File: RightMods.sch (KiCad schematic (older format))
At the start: 15 parts

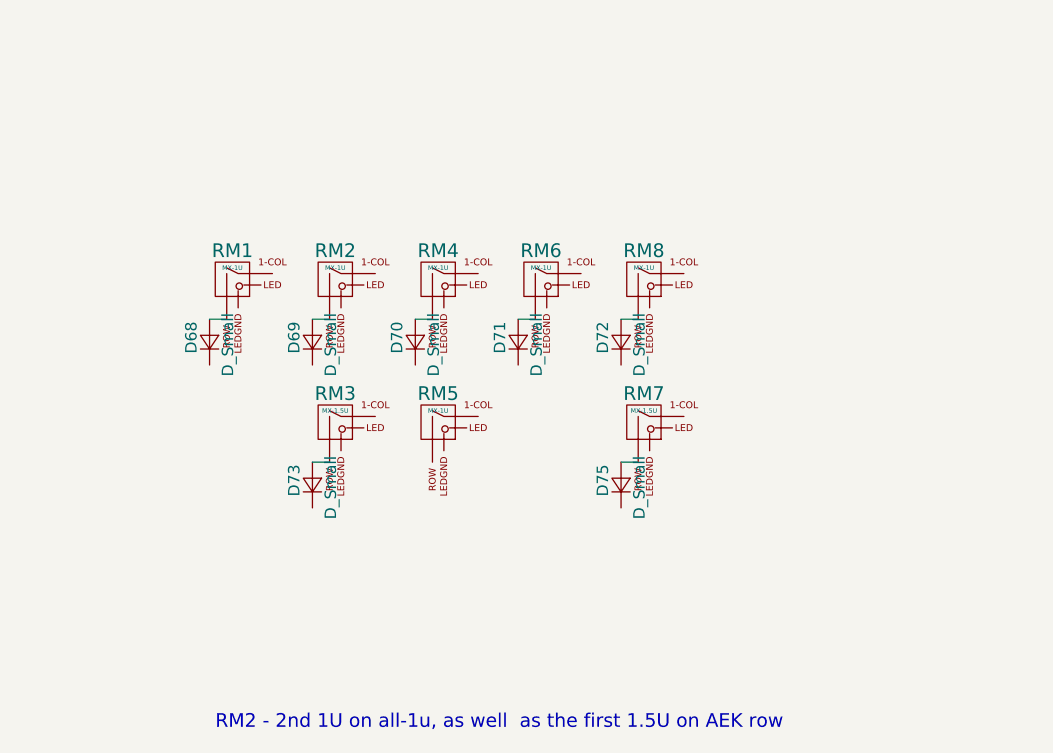
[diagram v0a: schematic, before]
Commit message: Place diodes, remove duplicates
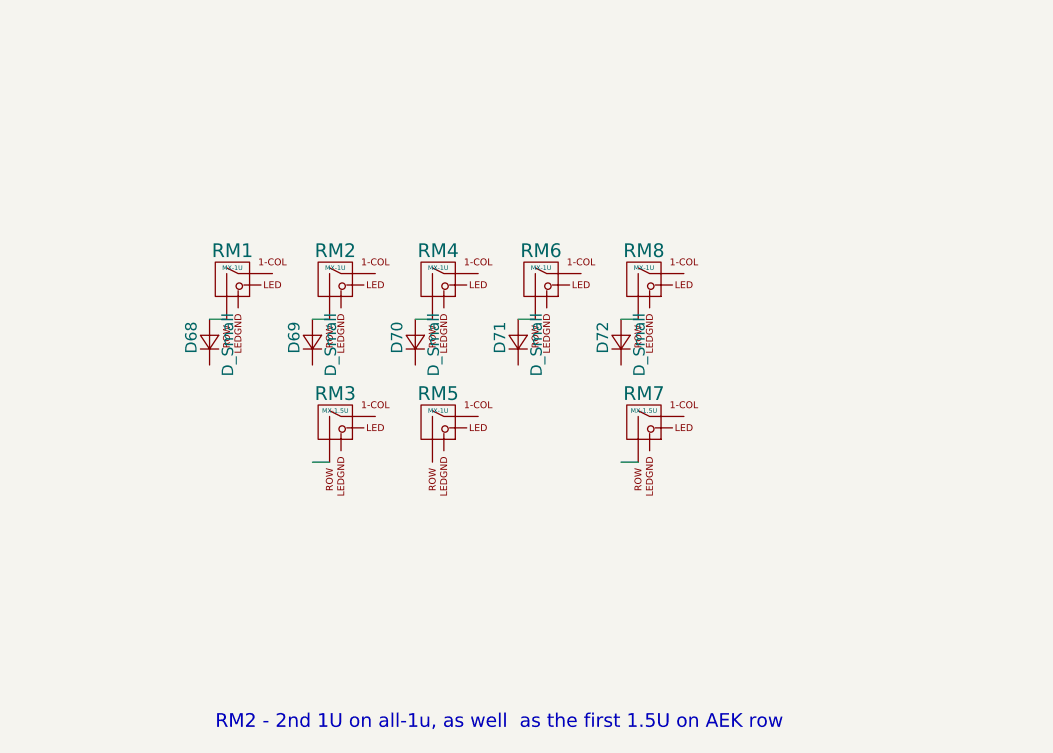
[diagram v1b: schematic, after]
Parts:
- removed D73, D75: D_Small, Diodes_SMD:D_SOD-123, symbol D_Small
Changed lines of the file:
@@
 	1    0    0    -1
-$EndComp
-$Comp
-L D_Small D73
-U 1 1 5A696AC3
-P 2525 3350
-F 0 "D73" H 2475 3430 50  0000 L CNN
-F 1 "D_Small" H 2375 3270 50  0000 L CNN
-F 2 "Diodes_SMD:D_SOD-123" V 2525 3350 50  0001 C CNN
-F 3 "" V 2525 3350 50  0001 C CNN
-	1    2525 3350
-	0    -1   -1   0
 $EndComp
 Wire Wire Line
@@
 	1    0    0    -1
 $EndComp
-$Comp
-L D_Small D75
-U 1 1 5A696AF0
-P 3875 3350
-F 0 "D75" H 3825 3430 50  0000 L CNN
-F 1 "D_Small" H 3725 3270 50  0000 L CNN
-F 2 "Diodes_SMD:D_SOD-123" V 3875 3350 50  0001 C CNN
-F 3 "" V 3875 3350 50  0001 C CNN
-	1    3875 3350
-	0    -1   -1   0
-$EndComp
 Wire Wire Line

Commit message: Add basic row col to subsheets
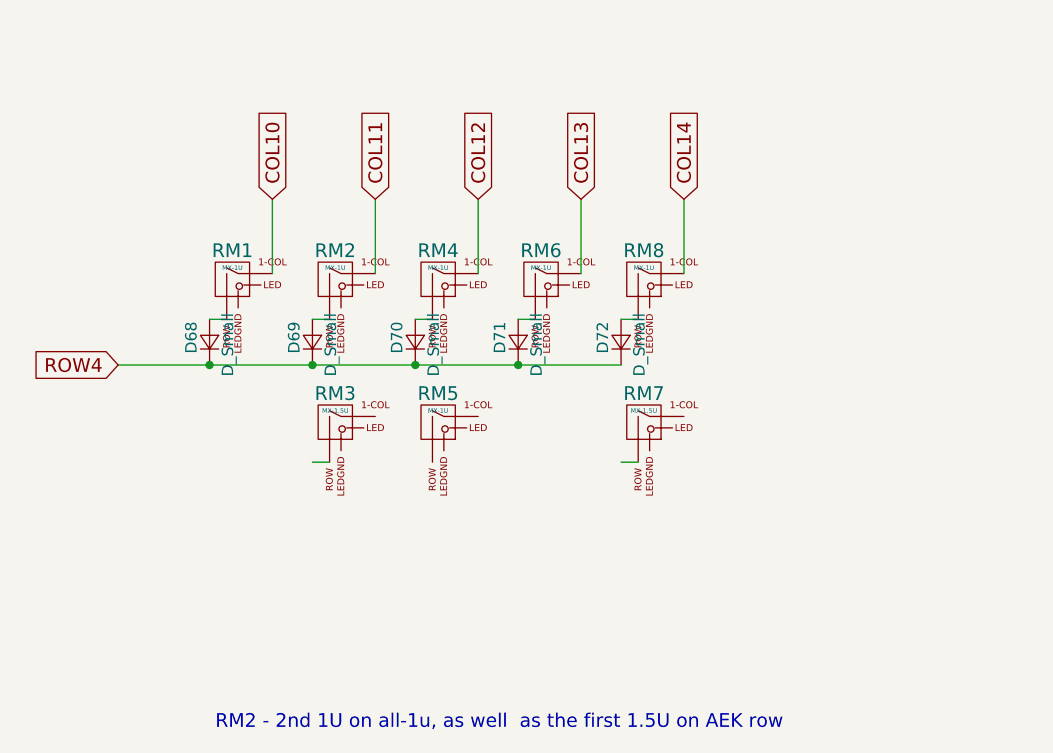
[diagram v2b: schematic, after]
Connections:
- net labels added: COL10, COL11, COL12, COL13, COL14, ROW4
- wire segments 7 -> 13
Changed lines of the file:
@@
 	1    0    0    -1
 $EndComp
+Wire Wire Line
+	4150 2425 4150 2100
+Text GLabel 4150 2100 1    60   Input ~ 0
+COL14
+Wire Wire Line
+	3700 2425 3700 2100
+Text GLabel 3700 2100 1    60   Input ~ 0
+COL13
+Wire Wire Line
+	3250 2425 3250 2100
+Text GLabel 3250 2100 1    60   Input ~ 0
+COL12
+Wire Wire Line
+	2800 2425 2800 2100
+Text GLabel 2800 2100 1    60   Input ~ 0
+COL11
+Wire Wire Line
+	2350 2425 2350 2100
+Text GLabel 2350 2100 1    60   Input ~ 0
+COL10
+Wire Wire Line
+	1675 2825 3875 2825
+Connection ~ 2525 2825
+Connection ~ 2975 2825
+Connection ~ 3425 2825
+Connection ~ 2075 2825
+Text GLabel 1675 2825 0    60   Input ~ 0
+ROW4
 $EndSCHEMATC

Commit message: Pinout right mods
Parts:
- RM3, RM7: footprint MX_Alps_Hybrid:MX-1.5U -> MX_Alps_Hybrid:MX-1.5U-FLIPPED
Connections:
- wire segments 13 -> 25
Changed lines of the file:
@@
 $EndComp
 Wire Wire Line
-	2600 2625 2525 2625
+	2400 2625 2600 2625
 $Comp
 L MX-1U RM4
@@
 $EndComp
 Wire Wire Line
-	3050 2625 2975 2625
+	2900 2625 3050 2625
 $Comp
 L MX-1U RM6
@@
 $EndComp
 Wire Wire Line
-	3950 2625 3875 2625
+	3750 2625 3950 2625
 $Comp
 L MX-1U RM3
@@
 F 0 "RM3" H 2625 3200 60  0000 C CNN
 F 1 "MX-1.5U" H 2625 3125 20  0000 C CNN
-F 2 "MX_Alps_Hybrid:MX-1.5U" H 2600 3050 60  0001 C CNN
+F 2 "MX_Alps_Hybrid:MX-1.5U-FLIPPED" H 2600 3050 60  0001 C CNN
 F 3 "" H 2600 3050 60  0001 C CNN
 	1    2625 3075
 	1    0    0    -1
 $EndComp
-Wire Wire Line
-	2600 3250 2525 3250
 $Comp
 L MX-1U RM7
@@
 F 0 "RM7" H 3975 3200 60  0000 C CNN
 F 1 "MX-1.5U" H 3975 3125 20  0000 C CNN
-F 2 "MX_Alps_Hybrid:MX-1.5U" H 3950 3050 60  0001 C CNN
+F 2 "MX_Alps_Hybrid:MX-1.5U-FLIPPED" H 3950 3050 60  0001 C CNN
 F 3 "" H 3950 3050 60  0001 C CNN
 	1    3975 3075
 	1    0    0    -1
 $EndComp
-Wire Wire Line
-	3950 3250 3875 3250
 Text Notes 2100 4425 0    60   ~ 0
 RM2 - 2nd 1U on all-1u, as well  as the first 1.5U on AEK row
@@
 COL13
 Wire Wire Line
-	3250 2425 3250 2100
+	3250 2100 3250 3050
 Text GLabel 3250 2100 1    60   Input ~ 0
 COL12
@@
 Text GLabel 1675 2825 0    60   Input ~ 0
 ROW4
+Wire Wire Line
+	2800 3050 2800 2900
+Wire Wire Line
+	2800 2900 2400 2900
+Wire Wire Line
+	2400 2900 2400 2625
+Connection ~ 2525 2625
+Wire Wire Line
+	2600 3250 2850 3250
+Wire Wire Line
+	2850 3250 2850 2425
+Wire Wire Line
+	2850 2425 2800 2425
+Connection ~ 3250 2425
+Wire Wire Line
+	3050 3250 2900 3250
+Wire Wire Line
+	2900 3250 2900 2625
+Connection ~ 2975 2625
+Wire Wire Line
+	4150 3050 4150 2900
+Wire Wire Line
+	4150 2900 3750 2900
+Wire Wire Line
+	3750 2900 3750 2625
+Connection ~ 3875 2625
+Wire Wire Line
+	3950 3250 4200 3250
+Wire Wire Line
+	4200 3250 4200 2425
+Wire Wire Line
+	4200 2425 4150 2425
 $EndSCHEMATC

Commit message: Swap footprints for No-LED counterparts
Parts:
- RM1, RM2, RM4, RM5, RM6, RM8: footprint MX_Alps_Hybrid:MX-1U -> MX_Alps_Hybrid:MX-1U-NoLED
- RM3, RM7: footprint MX_Alps_Hybrid:MX-1.5U-FLIPPED -> MX_Alps_Hybrid:MX-1.5U-NoLED
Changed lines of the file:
@@
 F 0 "RM1" H 2175 2575 60  0000 C CNN
 F 1 "MX-1U" H 2175 2500 20  0000 C CNN
-F 2 "MX_Alps_Hybrid:MX-1U" H 2150 2425 60  0001 C CNN
+F 2 "MX_Alps_Hybrid:MX-1U-NoLED" H 2150 2425 60  0001 C CNN
 F 3 "" H 2150 2425 60  0001 C CNN
 	1    2175 2450
@@
 F 0 "RM2" H 2625 2575 60  0000 C CNN
 F 1 "MX-1U" H 2625 2500 20  0000 C CNN
-F 2 "MX_Alps_Hybrid:MX-1U" H 2600 2425 60  0001 C CNN
+F 2 "MX_Alps_Hybrid:MX-1U-NoLED" H 2600 2425 60  0001 C CNN
 F 3 "" H 2600 2425 60  0001 C CNN
 	1    2625 2450
@@
 F 0 "RM4" H 3075 2575 60  0000 C CNN
 F 1 "MX-1U" H 3075 2500 20  0000 C CNN
-F 2 "MX_Alps_Hybrid:MX-1U" H 3050 2425 60  0001 C CNN
+F 2 "MX_Alps_Hybrid:MX-1U-NoLED" H 3050 2425 60  0001 C CNN
 F 3 "" H 3050 2425 60  0001 C CNN
 	1    3075 2450
@@
 F 0 "RM6" H 3525 2575 60  0000 C CNN
 F 1 "MX-1U" H 3525 2500 20  0000 C CNN
-F 2 "MX_Alps_Hybrid:MX-1U" H 3500 2425 60  0001 C CNN
+F 2 "MX_Alps_Hybrid:MX-1U-NoLED" H 3500 2425 60  0001 C CNN
 F 3 "" H 3500 2425 60  0001 C CNN
 	1    3525 2450
@@
 F 0 "RM8" H 3975 2575 60  0000 C CNN
 F 1 "MX-1U" H 3975 2500 20  0000 C CNN
-F 2 "MX_Alps_Hybrid:MX-1U" H 3950 2425 60  0001 C CNN
+F 2 "MX_Alps_Hybrid:MX-1U-NoLED" H 3950 2425 60  0001 C CNN
 F 3 "" H 3950 2425 60  0001 C CNN
 	1    3975 2450
@@
 F 0 "RM3" H 2625 3200 60  0000 C CNN
 F 1 "MX-1.5U" H 2625 3125 20  0000 C CNN
-F 2 "MX_Alps_Hybrid:MX-1.5U-FLIPPED" H 2600 3050 60  0001 C CNN
+F 2 "MX_Alps_Hybrid:MX-1.5U-NoLED" H 2600 3050 60  0001 C CNN
 F 3 "" H 2600 3050 60  0001 C CNN
 	1    2625 3075
@@
 F 0 "RM7" H 3975 3200 60  0000 C CNN
 F 1 "MX-1.5U" H 3975 3125 20  0000 C CNN
-F 2 "MX_Alps_Hybrid:MX-1.5U-FLIPPED" H 3950 3050 60  0001 C CNN
+F 2 "MX_Alps_Hybrid:MX-1.5U-NoLED" H 3950 3050 60  0001 C CNN
 F 3 "" H 3950 3050 60  0001 C CNN
 	1    3975 3075
@@
 F 0 "RM5" H 3075 3200 60  0000 C CNN
 F 1 "MX-1U" H 3075 3125 20  0000 C CNN
-F 2 "MX_Alps_Hybrid:MX-1U" H 3050 3050 60  0001 C CNN
+F 2 "MX_Alps_Hybrid:MX-1U-NoLED" H 3050 3050 60  0001 C CNN
 F 3 "" H 3050 3050 60  0001 C CNN
 	1    3075 3075

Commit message: Update right mods
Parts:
- removed D68, D69, D70, D71, D72: D_Small, Diodes_SMD:D_SOD-123, symbol D_Small
- added RM9: MX-1U, symbol MX-1U
- RM1, RM2, RM4, RM5, RM6, RM8: footprint MX_Alps_Hybrid:MX-1U-NoLED -> (none)
- RM3, RM7: value MX-1.5U -> MX-1U; footprint MX_Alps_Hybrid:MX-1.5U-NoLED -> (none)
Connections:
- net COL11: no longer RM3.2 (ROW)
- net COL12: no longer RM5.1 (COL)
- net COL13: now also RM7.1 (COL); no longer RM6.1 (COL)
- net COL14: now also RM9.1 (COL); no longer RM7.2 (ROW), RM8.1 (COL)
- net ROW4: now also RM2.2 (ROW), RM4.2 (ROW), RM7.2 (ROW), RM9.2 (ROW)
- net at RM3.1 (COL): no longer RM2.2 (ROW)
- net at RM5.2 (ROW): no longer RM4.2 (ROW)
- net at RM8.2 (ROW): no longer RM7.1 (COL)
- net COL10: no longer names the net of RM1.1 (COL)
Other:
- note removed: "RM2 - 2nd 1U on all-1u, as well as the first 1.5U on AEK row"

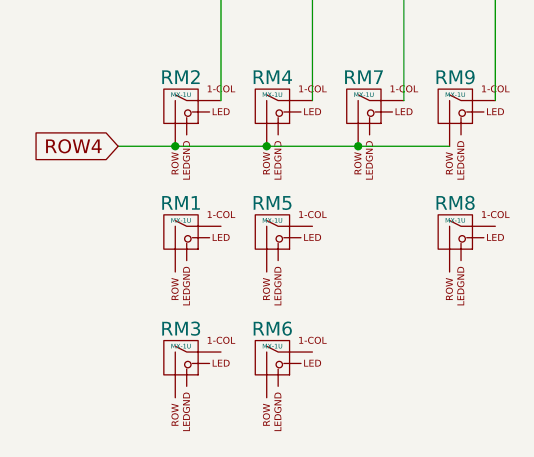
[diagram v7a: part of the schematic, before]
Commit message: Assign footprints to updated mods
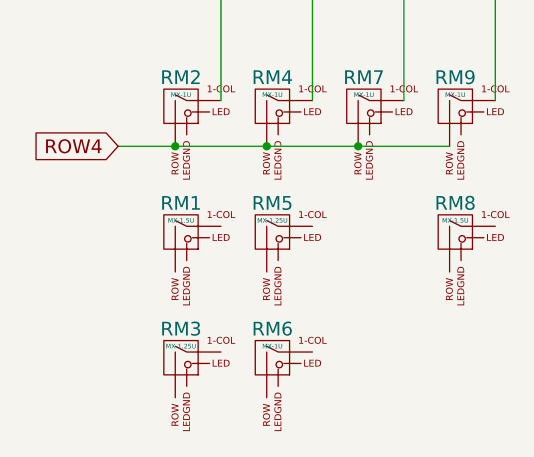
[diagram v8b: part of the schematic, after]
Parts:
- RM1, RM8: value MX-1U -> MX-1.5U; footprint (none) -> MX_Alps_Hybrid:MX-1.5U-NoLED
- RM2, RM4, RM6, RM7, RM9: footprint (none) -> MX_Alps_Hybrid:MX-1U-NoLED
- RM3, RM5: value MX-1U -> MX-1.25U; footprint (none) -> MX_Alps_Hybrid:MX-1.25U-NoLED
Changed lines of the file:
@@
 F 0 "RM2" H 2450 2425 60  0000 C CNN
 F 1 "MX-1U" H 2450 2350 20  0000 C CNN
-F 2 "" H 2425 2275 60  0001 C CNN
+F 2 "MX_Alps_Hybrid:MX-1U-NoLED" H 2425 2275 60  0001 C CNN
 F 3 "" H 2425 2275 60  0001 C CNN
 	1    2450 2300
@@
 P 2450 2850
 F 0 "RM1" H 2450 2975 60  0000 C CNN
-F 1 "MX-1U" H 2450 2900 20  0000 C CNN
-F 2 "" H 2425 2825 60  0001 C CNN
+F 1 "MX-1.5U" H 2450 2900 20  0000 C CNN
+F 2 "MX_Alps_Hybrid:MX-1.5U-NoLED" H 2425 2825 60  0001 C CNN
 F 3 "" H 2425 2825 60  0001 C CNN
 	1    2450 2850
@@
 P 2450 3400
 F 0 "RM3" H 2450 3525 60  0000 C CNN
-F 1 "MX-1U" H 2450 3450 20  0000 C CNN
-F 2 "" H 2425 3375 60  0001 C CNN
+F 1 "MX-1.25U" H 2450 3450 20  0000 C CNN
+F 2 "MX_Alps_Hybrid:MX-1.25U-NoLED" H 2425 3375 60  0001 C CNN
 F 3 "" H 2425 3375 60  0001 C CNN
 	1    2450 3400
@@
 F 0 "RM4" H 2850 2425 60  0000 C CNN
 F 1 "MX-1U" H 2850 2350 20  0000 C CNN
-F 2 "" H 2825 2275 60  0001 C CNN
+F 2 "MX_Alps_Hybrid:MX-1U-NoLED" H 2825 2275 60  0001 C CNN
 F 3 "" H 2825 2275 60  0001 C CNN
 	1    2850 2300
@@
 P 2850 2850
 F 0 "RM5" H 2850 2975 60  0000 C CNN
-F 1 "MX-1U" H 2850 2900 20  0000 C CNN
-F 2 "" H 2825 2825 60  0001 C CNN
+F 1 "MX-1.25U" H 2850 2900 20  0000 C CNN
+F 2 "MX_Alps_Hybrid:MX-1.25U-NoLED" H 2825 2825 60  0001 C CNN
 F 3 "" H 2825 2825 60  0001 C CNN
 	1    2850 2850
@@
 F 0 "RM7" H 3250 2425 60  0000 C CNN
 F 1 "MX-1U" H 3250 2350 20  0000 C CNN
-F 2 "" H 3225 2275 60  0001 C CNN
+F 2 "MX_Alps_Hybrid:MX-1U-NoLED" H 3225 2275 60  0001 C CNN
 F 3 "" H 3225 2275 60  0001 C CNN
 	1    3250 2300
@@
 F 0 "RM9" H 3650 2425 60  0000 C CNN
 F 1 "MX-1U" H 3650 2350 20  0000 C CNN
-F 2 "" H 3625 2275 60  0001 C CNN
+F 2 "MX_Alps_Hybrid:MX-1U-NoLED" H 3625 2275 60  0001 C CNN
 F 3 "" H 3625 2275 60  0001 C CNN
 	1    3650 2300
@@
 F 0 "RM6" H 2850 3525 60  0000 C CNN
 F 1 "MX-1U" H 2850 3450 20  0000 C CNN
-F 2 "" H 2825 3375 60  0001 C CNN
+F 2 "MX_Alps_Hybrid:MX-1U-NoLED" H 2825 3375 60  0001 C CNN
 F 3 "" H 2825 3375 60  0001 C CNN
 	1    2850 3400
@@
 P 3650 2850
 F 0 "RM8" H 3650 2975 60  0000 C CNN
-F 1 "MX-1U" H 3650 2900 20  0000 C CNN
-F 2 "" H 3625 2825 60  0001 C CNN
+F 1 "MX-1.5U" H 3650 2900 20  0000 C CNN
+F 2 "MX_Alps_Hybrid:MX-1.5U-NoLED" H 3625 2825 60  0001 C CNN
 F 3 "" H 3625 2825 60  0001 C CNN
 	1    3650 2850
